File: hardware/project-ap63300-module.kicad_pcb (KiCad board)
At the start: 2 copper layers, 20.3 x 16.5 mm, 14 parts, among them J1 Conn_01x02_Male, J2 Conn_01x02_Male, J3 Conn_01x02_Male, U1 AP63300WU-7

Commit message: Open with kicad 8
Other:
- net class Default removed

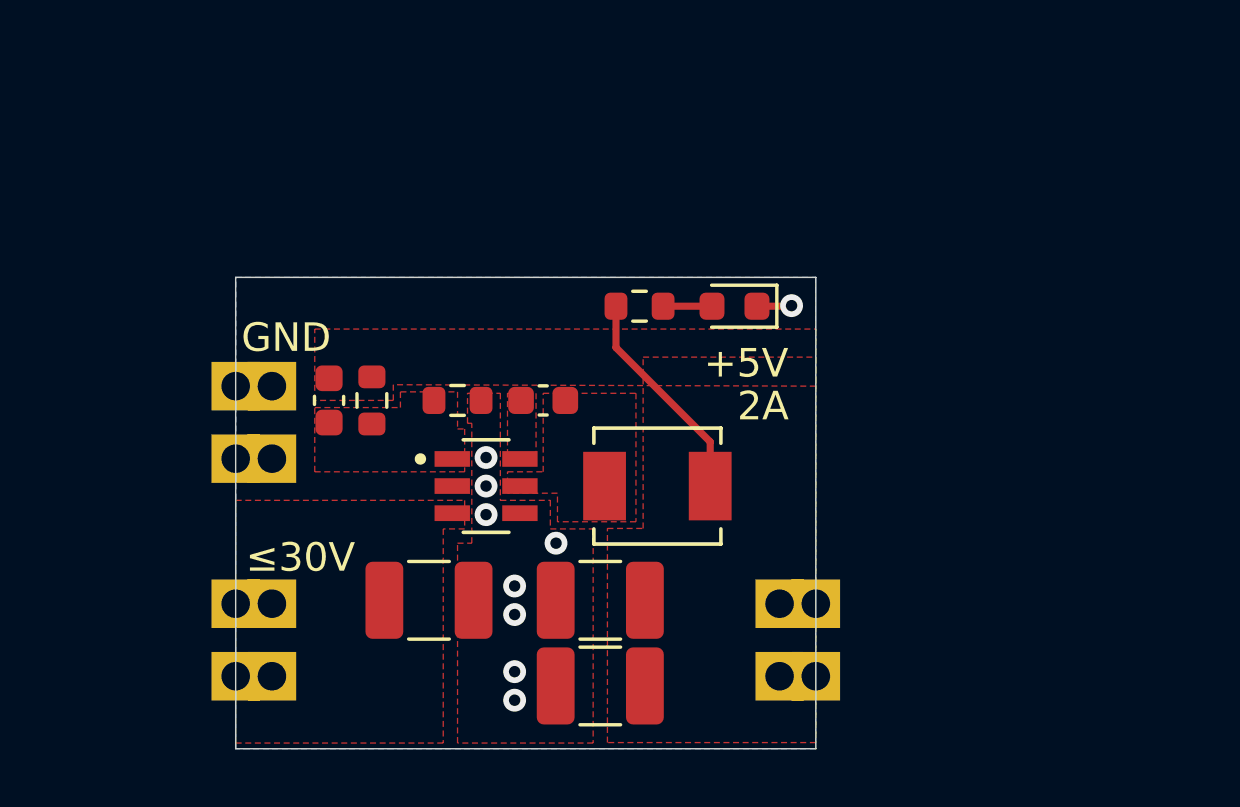
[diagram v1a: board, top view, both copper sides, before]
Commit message: pcb: first placement
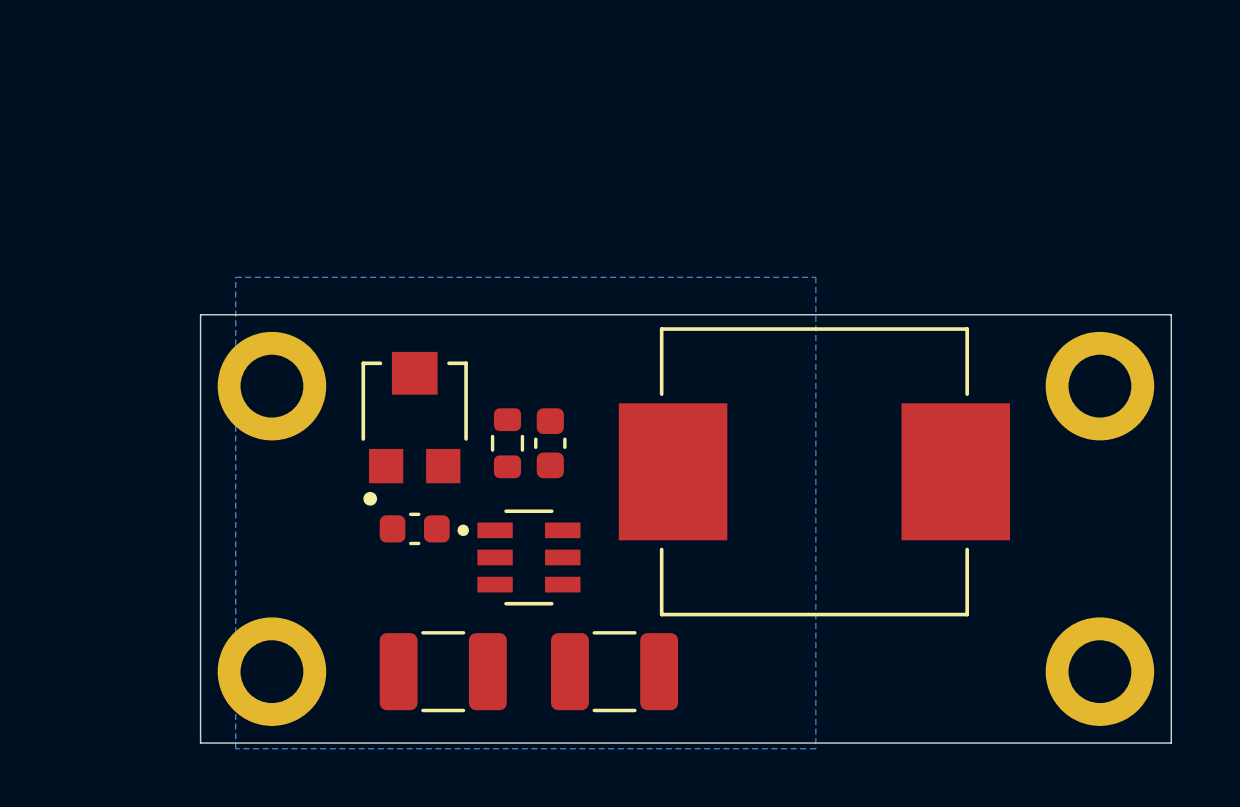
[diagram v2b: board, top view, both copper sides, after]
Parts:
- removed C5: 22uF, Capacitor_SMD:C_1210_3225Metric_Pad1.33x2.70mm_HandSolder
- removed D1: LED, LED_SMD:LED_0603_1608Metric
- removed J1, J2, J3: Conn_01x02_Male, Connector_PinHeader_2.54mm:PinHeader_1x02_P2.54mm_Vertical
- removed R6: 10k, Resistor_SMD:R_0603_1608Metric
- removed U1: AP63300WU-7, AP63300WU-7:SOT95P280X100-6N
- added H1: MountingHole_Pad, MountingHole:MountingHole_2.2mm_M2_ISO14580_Pad, F.Cu at (20.6, 34.5)
- added H2: MountingHole_Pad, MountingHole:MountingHole_2.2mm_M2_ISO14580_Pad, F.Cu at (49.6, 34.5)
- added H3: MountingHole_Pad, MountingHole:MountingHole_2.2mm_M2_ISO14580_Pad, F.Cu at (20.6, 24.5)
- added H4: MountingHole_Pad, MountingHole:MountingHole_2.2mm_M2_ISO14580_Pad, F.Cu at (49.6, 24.5)
- added U2: AP63300WU-7, AP63300WU-7:SOT95P280X100-6N, F.Cu at (29.6, 30.5)
- L1: value 6.8uH -> 10uH; footprint SRP4020TA-6R8M:IND_SRP4020TA-6R8M -> SPM10040T_100M:IND_SPM10040T-100M
- R2: value 158k -> TC33X-2-504E; footprint Resistor_SMD:R_0603_1608Metric -> TC33X_2_504E:TRIM_TC33X-2-504E
- R3: value 30.1k -> 17.2k
- moved L1 5.52 mm to (39.6, 27.5)
- moved C3 5.41 mm to (25.6, 29.5), turned to 0 degrees
- moved C1 2.55 mm to (26.6, 34.5)
- moved R3 2.30 mm to (28.8, 26.5), turned to -90 degrees
- moved R2 1.58 mm to (25.6, 25.5), turned to 90 degrees
- moved C2 1.52 mm to (30.3, 26.5), turned to 90 degrees
- moved C4 0.71 mm to (32.6, 34.5)
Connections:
- net +5V renamed Vout
- net Net-(C2-Pad2) renamed /sw
- C1 pad 1: +12V -> Vin
- C2 pad 1: Net-(C2-Pad1) -> /BST
- C3 pad 2: Net-(C3-Pad2) -> /FB
- R2 pad 2: Net-(C3-Pad2) -> /FB
- R3 pad 1: Net-(C3-Pad2) -> /FB
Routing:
- net Vout: track 7.67 -> 0.00 mm
- net Net-(D1-Pad2): track 1.71 -> 0.00 mm
- net GND: track 1.22 -> 0.00 mm, vias 9 -> 0
- removed copper zone on F.Cu, net +12V
- removed copper zone on F.Cu, net /sw
- removed copper zone on F.Cu, net GND
- removed copper zone on F.Cu, net Net-(C2-Pad1)
- removed copper zone on F.Cu, net Net-(C3-Pad2)
- removed copper zone on F.Cu, net Vout
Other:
- board size 20.3 x 16.5 mm -> 34 x 15 mm
- board text removed: "+5V"
- board text removed: "2A"
- board text removed: "François Gervais 11 Avril 2021 rev"
- board text removed: "GND"
- board text removed: "≤30V"

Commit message: pcb: first routing draft
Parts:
- moved H2 12.0 mm to (41.6, 25.5)
- moved C4 10.3 mm to (27.6, 25.5)
- moved C1 10.3 mm to (21.6, 25.5)
- moved H1 10.3 mm to (15.6, 25.5)
- moved C2 10.3 mm to (25.3, 17.5)
- moved C3 10.3 mm to (20.6, 20.5)
- moved L1 10.3 mm to (34.6, 18.5)
- moved R2 10.3 mm to (20.6, 16.5)
- moved R3 10.3 mm to (23.8, 17.5)
- moved U2 10.3 mm to (24.6, 21.5)
- moved H3 10.3 mm to (15.6, 15.5)
- moved H4 9.06 mm to (50.6, 15.5)
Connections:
- net /sw renamed /SW
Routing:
- net Vout: track 0.00 -> 20.5 mm, vias 0 -> 2
- net /BST: track 0.00 -> 2.46 mm
- net GND: vias 0 -> 22
- added copper zone on F.Cu, net /FB
- added copper zone on F.Cu, net /SW
- added copper zone on F.Cu, net GND
- added copper zone on F.Cu, net Vin
- added copper zone on F.Cu, net Vout
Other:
- board size 34 x 15 mm -> 31 x 15 mm

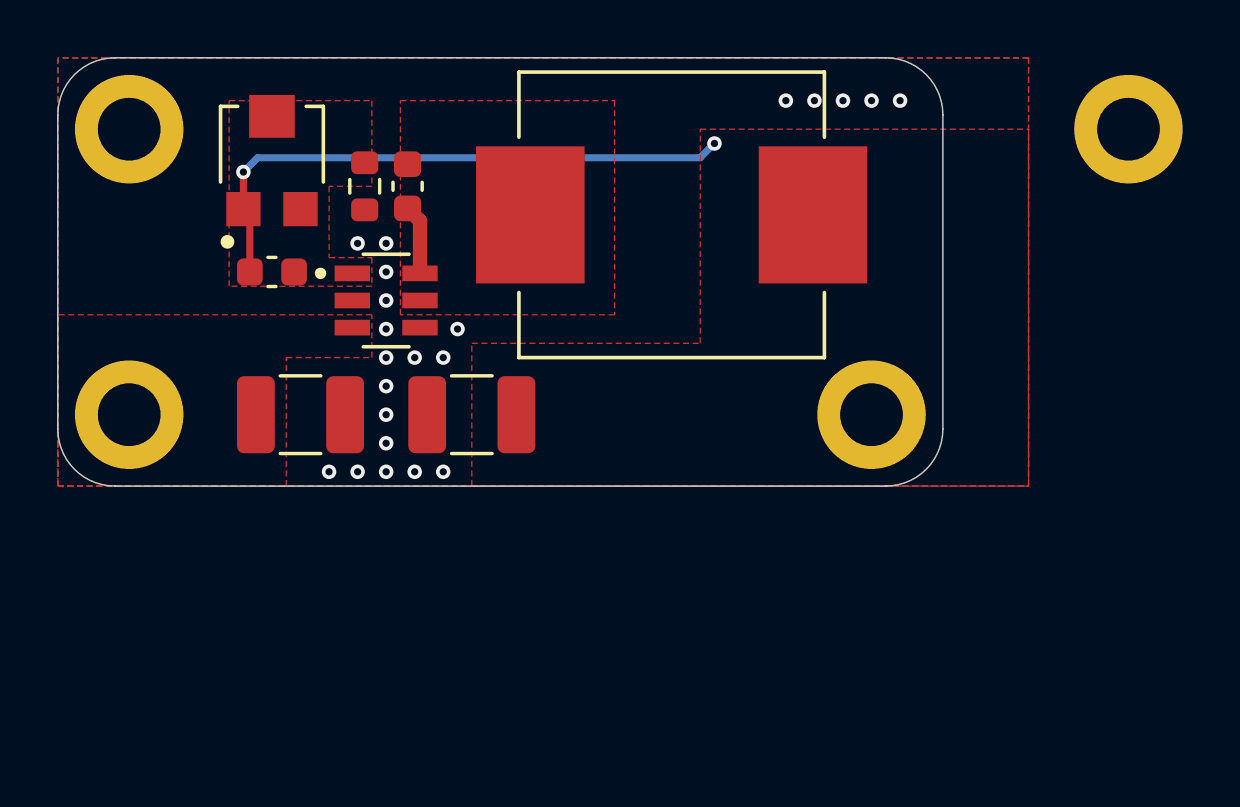
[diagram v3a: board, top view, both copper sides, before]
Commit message: Add labels
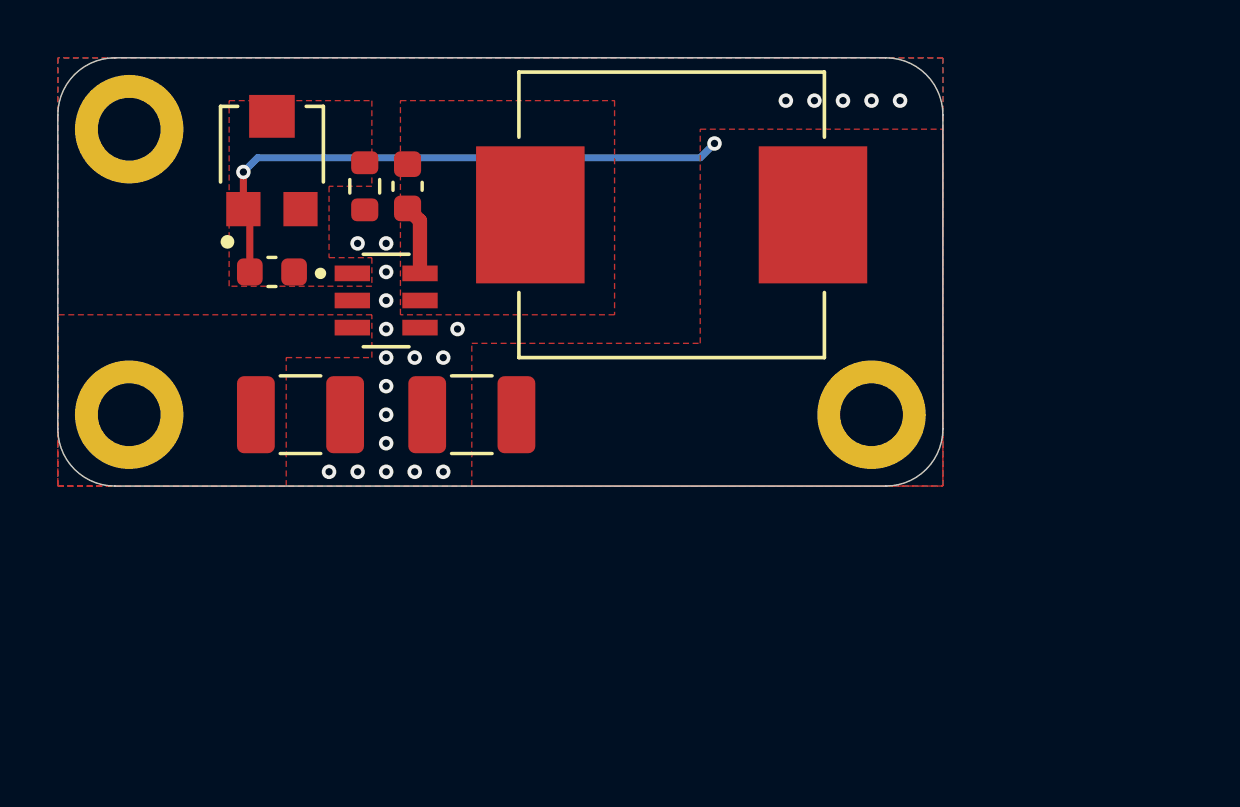
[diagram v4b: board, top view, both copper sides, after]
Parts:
- removed H4: MountingHole_Pad, MountingHole:MountingHole_2.2mm_M2_ISO14580_Pad
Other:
- board text added: "5 janvier 2024"
- board text added: "Gnd"
- board text added: "Vin"
- board text added: "Vout"
